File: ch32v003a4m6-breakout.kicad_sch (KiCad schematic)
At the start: 4 parts, among them J1 Conn_01x08, J2 Conn_01x08, U1 CH32V003A4M6

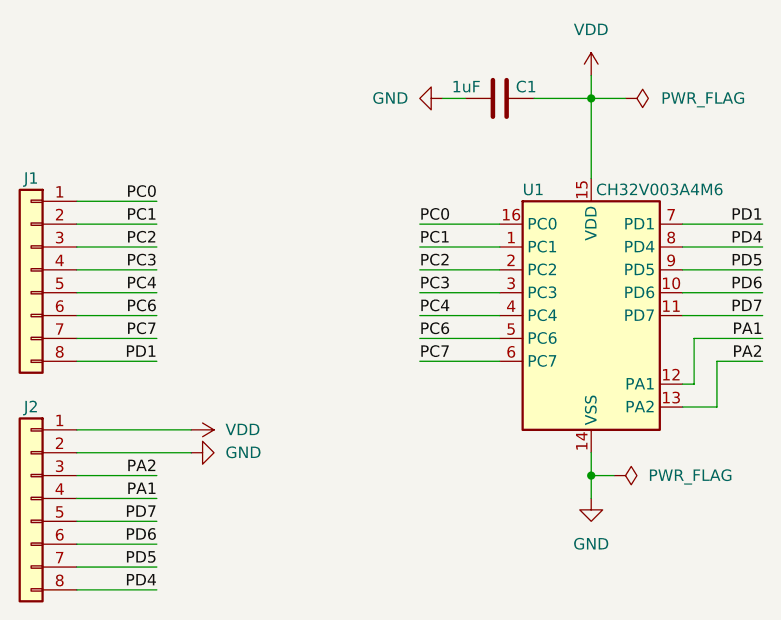
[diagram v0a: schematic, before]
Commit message: fix: use default KiCad libraries
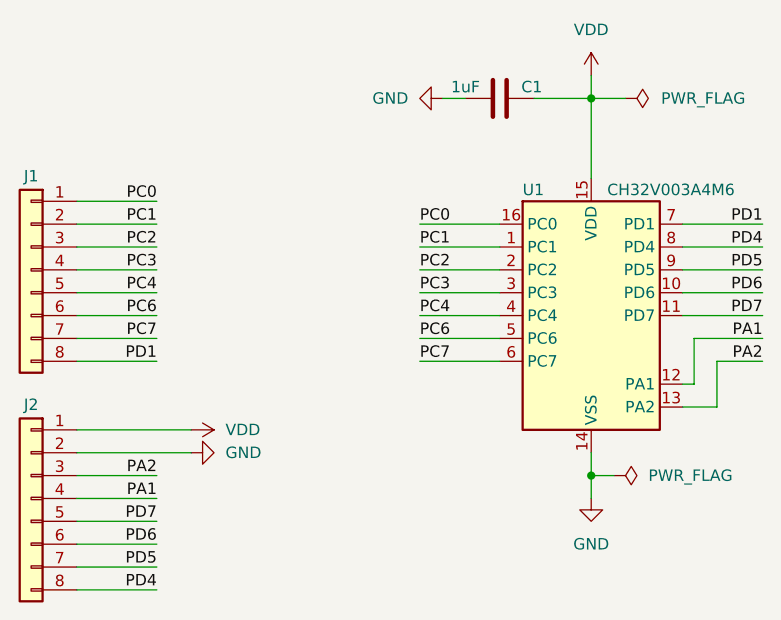
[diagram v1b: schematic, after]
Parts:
- removed C1: CL10A105KA8NNNC, Capacitor_SMD:C_0603_1608Metric, symbol Capacitor:CL10A105KA8NNNC
- removed J1, J2: Conn_01x08, Connector_PinHeader:PinHeader_1x08_P2.54mm_Vertical, symbol Connector:Conn_01x08
- removed U1: CH32V003A4M6, Package_SO:SOP-16_3.9x9.9mm_P1.27mm, symbol MCU_WCH:CH32V003A4M6
- added C1: 1uF, Capacitor_SMD:C_0603_1608Metric, symbol Device:C
- added J1, J2: Conn_01x08, Connector_PinHeader_2.54mm:PinHeader_1x08_P2.54mm_Vertical, symbol Connector_Generic:Conn_01x08
- added U1: CH32V003A4M6, Package_SO:SOP-16_3.9x9.9mm_P1.27mm, symbol MCU_WCH_CH32V0:CH32V003AxMx
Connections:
- net GND: now also C1.1, J2.2 (Pin_2), U1.14 (VSS)
- net PA1: now also J2.4 (Pin_4), U1.12 (PA1)
- net PA2: now also J2.3 (Pin_3), U1.13 (PA2)
- net PC0: now also J1.1 (Pin_1), U1.16 (PC0)
- net PC1: now also J1.2 (Pin_2), U1.1 (PC1)
- net PC2: now also J1.3 (Pin_3), U1.2 (PC2)
- net PC3: now also J1.4 (Pin_4), U1.3 (PC3)
- net PC4: now also J1.5 (Pin_5), U1.4 (PC4)
- net PC6: now also J1.6 (Pin_6), U1.5 (PC6)
- net PC7: now also J1.7 (Pin_7), U1.6 (PC7)
- net PD1: now also J1.8 (Pin_8), U1.7 (PD1)
- net PD4: now also J2.8 (Pin_8), U1.8 (PD4)
- net PD5: now also J2.7 (Pin_7), U1.9 (PD5)
- net PD6: now also J2.6 (Pin_6), U1.10 (PD6)
- net PD7: now also J2.5 (Pin_5), U1.11 (PD7)
- net VDD: now also C1.2, J2.1 (Pin_1), U1.15 (VDD)
